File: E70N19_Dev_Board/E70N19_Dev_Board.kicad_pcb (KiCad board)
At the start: 2 copper layers, 88.9 x 83.8 mm, 79 parts, among them J1 USB_microB_2040002-1, J2 Battery 1x2, J3 JTAGSEL_JUMPER 1x3, J4 UART_PROG 1x2, J5 ERASE_JUMPER 1x3, J6 ARM-Cortex-Debug-10, J7 CAN 1x2, J8 Conn_02x15_Counter_Clockwise, J9 Conn_02x15_Counter_Clockwise, SW1 NRST_BUTTON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

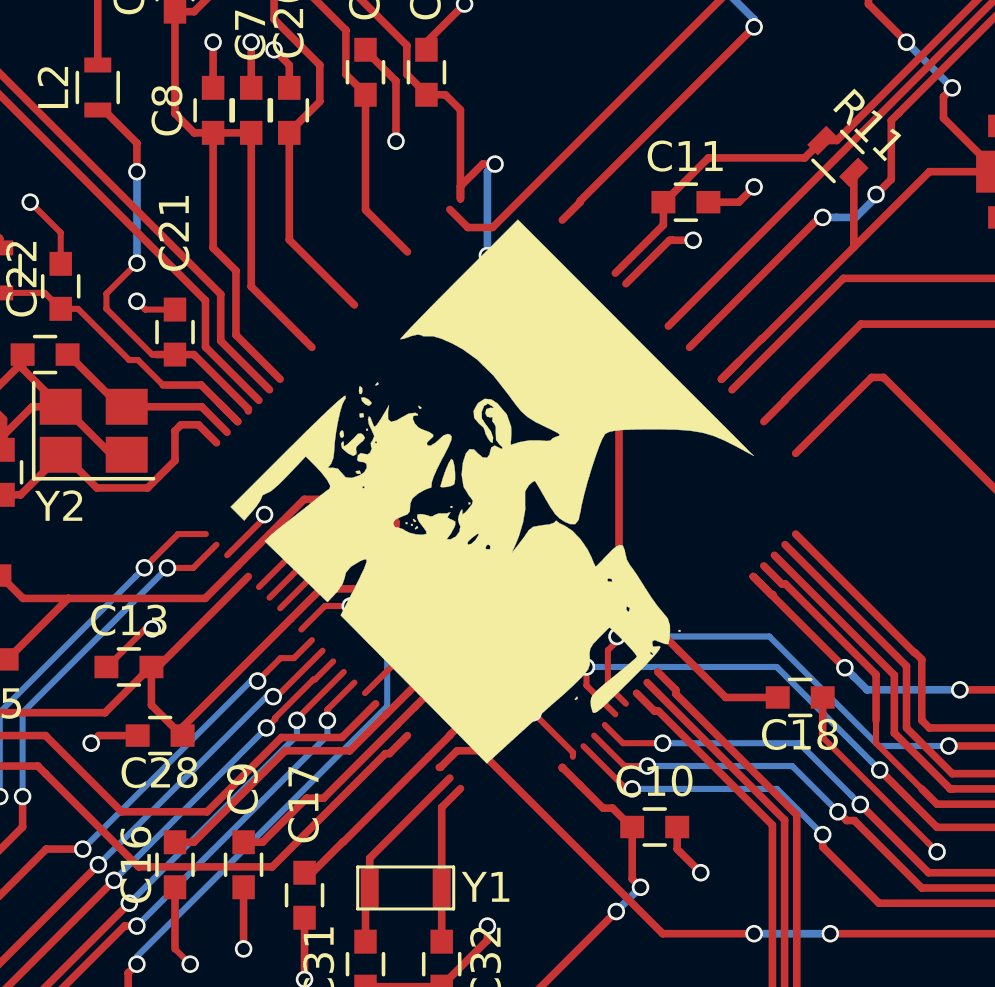
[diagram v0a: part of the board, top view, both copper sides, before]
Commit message: Fixing missing uC footprint
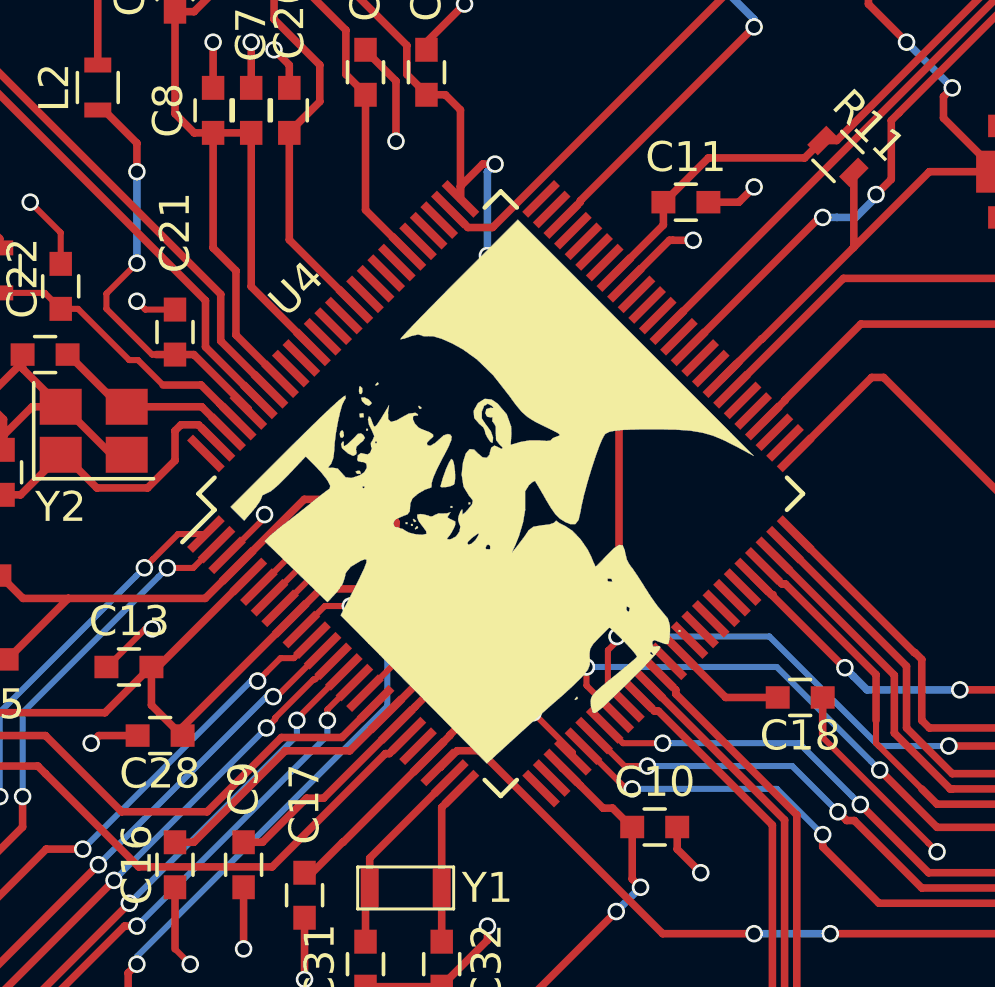
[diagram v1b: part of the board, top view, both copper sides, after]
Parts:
- added U4: ATSAME70N19, Housings_QFP:LQFP-100_14x14mm_Pitch0.5mm, F.Cu at (129.0, 70.7)

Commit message: No rat lines
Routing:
- net GND: track 128.6 -> 145.6 mm, vias 51 -> 58
- net (no net): track 17.0 -> 0.00 mm, vias 7 -> 0
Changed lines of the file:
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@@
-(kicad_pcb (version 4) (host pcbnew 4.0.2+dfsg1-stable)
+(kicad_pcb (version 4) (host pcbnew 4.0.7)
   (general
     (links 204)
-    (no_connects 61)
-    (area 83.744999 25.324999 172.795001 109.295001)
+    (no_connects 0)
+    (area 81.28 22.86 185.420001 116.840001)
     (thickness 1.6)
     (drawings 9)
@@
   (gr_arc (start 170.18 106.68) (end 172.72 106.68) (angle 90) (layer Edge.Cuts) (width 0.15))
   (gr_arc (start 170.18 27.94) (end 170.18 25.4) (angle 90) (layer Edge.Cuts) (width 0.15))
-  (segment (start 120.907718 73.790256) (end 122.033244 72.66473) (width 0.2032) (layer F.Cu) (net 0))
-  (segment (start 122.033244 72.66473) (end 122.033244 72.471845) (width 0.2032) (layer F.Cu) (net 0))
-  (via (at 122.033244 72.058754) (size 0.5842) (drill 0.4064) (layers F.Cu B.Cu) (net 0))
-  (segment (start 122.033244 72.471845) (end 122.033244 72.058754) (width 0.2032) (layer F.Cu) (net 0))
-  (segment (start 119.847058 72.729596) (end 121.09449 71.482164) (width 0.2032) (layer F.Cu) (net 0))
-  (via (at 121.09449 71.374) (size 0.5842) (drill 0.4064) (layers F.Cu B.Cu) (net 0))
-  (segment (start 121.09449 71.482164) (end 121.09449 71.374) (width 0.2032) (layer F.Cu) (net 0))
-  (segment (start 131.372898 79.44711) (end 131.372898 79.302898) (width 0.2032) (layer F.Cu) (net 0))
-  (segment (start 131.372898 79.302898) (end 130.048 77.978) (width 0.2032) (layer F.Cu) (net 0))
-  (via (at 130.048 77.978) (size 0.5842) (drill 0.4064) (layers F.Cu B.Cu) (net 0))
-  (via (at 123.952 74.422) (size 0.5842) (drill 0.4064) (layers F.Cu B.Cu) (net 0))
-  (segment (start 123.1044 74.422) (end 123.952 74.422) (width 0.2032) (layer F.Cu) (net 0))
-  (segment (start 122.321931 75.204469) (end 123.1044 74.422) (width 0.2032) (layer F.Cu) (net 0))
-  (segment (start 121.614824 74.497363) (end 124.206 71.906187) (width 0.2032) (layer F.Cu) (net 0))
-  (segment (start 124.206 71.906187) (end 124.206 71.882) (width 0.2032) (layer F.Cu) (net 0))
-  (via (at 124.206 71.882) (size 0.5842) (drill 0.4064) (layers F.Cu B.Cu) (net 0))
-  (segment (start 121.261271 74.143809) (end 122.936 72.46908) (width 0.2032) (layer F.Cu) (net 0))
-  (segment (start 122.936 72.46908) (end 122.936 72.39) (width 0.2032) (layer F.Cu) (net 0))
-  (via (at 122.936 72.39) (size 0.5842) (drill 0.4064) (layers F.Cu B.Cu) (net 0))
-  (segment (start 133.140665 63.678629) (end 134.589294 62.23) (width 0.254) (layer F.Cu) (net 0))
-  (segment (start 134.589294 62.23) (end 134.703264 62.23) (width 0.254) (layer F.Cu) (net 0))
-  (segment (start 134.703264 62.23) (end 135.382 62.23) (width 0.254) (layer F.Cu) (net 0))
-  (via (at 135.382 62.23) (size 0.5842) (drill 0.4064) (layers F.Cu B.Cu) (net 0))
+  (segment (start 120.907718 73.790256) (end 122.033244 72.66473) (width 0.2032) (layer F.Cu) (net 1))
+  (segment (start 122.033244 72.66473) (end 122.033244 72.471845) (width 0.2032) (layer F.Cu) (net 1))
+  (via (at 122.033244 72.058754) (size 0.5842) (drill 0.4064) (layers F.Cu B.Cu) (net 1))
+  (segment (start 122.033244 72.471845) (end 122.033244 72.058754) (width 0.2032) (layer F.Cu) (net 1))
+  (segment (start 119.847058 72.729596) (end 121.09449 71.482164) (width 0.2032) (layer F.Cu) (net 1))
+  (via (at 121.09449 71.374) (size 0.5842) (drill 0.4064) (layers F.Cu B.Cu) (net 1))
+  (segment (start 121.09449 71.482164) (end 121.09449 71.374) (width 0.2032) (layer F.Cu) (net 1))
+  (segment (start 131.372898 79.44711) (end 131.372898 79.302898) (width 0.2032) (layer F.Cu) (net 1))
+  (segment (start 131.372898 79.302898) (end 130.048 77.978) (width 0.2032) (layer F.Cu) (net 1))
+  (via (at 130.048 77.978) (size 0.5842) (drill 0.4064) (layers F.Cu B.Cu) (net 1))
+  (via (at 123.952 74.422) (size 0.5842) (drill 0.4064) (layers F.Cu B.Cu) (net 1))
+  (segment (start 123.1044 74.422) (end 123.952 74.422) (width 0.2032) (layer F.Cu) (net 1))
+  (segment (start 122.321931 75.204469) (end 123.1044 74.422) (width 0.2032) (layer F.Cu) (net 1))
+  (segment (start 121.614824 74.497363) (end 124.206 71.906187) (width 0.2032) (layer F.Cu) (net 1))
+  (segment (start 124.206 71.906187) (end 124.206 71.882) (width 0.2032) (layer F.Cu) (net 1))
+  (via (at 124.206 71.882) (size 0.5842) (drill 0.4064) (layers F.Cu B.Cu) (net 1))
+  (segment (start 121.261271 74.143809) (end 122.936 72.46908) (width 0.2032) (layer F.Cu) (net 1))
+  (segment (start 122.936 72.46908) (end 122.936 72.39) (width 0.2032) (layer F.Cu) (net 1))
+  (via (at 122.936 72.39) (size 0.5842) (drill 0.4064) (layers F.Cu B.Cu) (net 1))
+  (segment (start 133.140665 63.678629) (end 134.589294 62.23) (width 0.254) (layer F.Cu) (net 1))
+  (segment (start 134.589294 62.23) (end 134.703264 62.23) (width 0.254) (layer F.Cu) (net 1))
+  (segment (start 134.703264 62.23) (end 135.382 62.23) (width 0.254) (layer F.Cu) (net 1))
+  (via (at 135.382 62.23) (size 0.5842) (drill 0.4064) (layers F.Cu B.Cu) (net 1))
   (segment (start 118.11 85.852) (end 118.618 86.36) (width 0.2032) (layer F.Cu) (net 1))
   (via (at 118.618 86.36) (size 0.5842) (drill 0.4064) (layers F.Cu B.Cu) (net 1))
